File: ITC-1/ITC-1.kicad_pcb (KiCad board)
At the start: 4 copper layers, 46 x 46 mm, 71 parts, among them K1 кнопка, K2 кнопка, X1 крепеж, X2 крепеж, X3 крепеж, X4 крепеж

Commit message: закончена трассировка, сформированы герберы
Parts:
- added C3: Конденсатор_керамический, N_RLC:Конденсатор_SMD_0603_pnp, F.Cu at (87.5, 86.8)
- added C4: Конденсатор_керамический, N_RLC:Конденсатор_SMD_0603_pnp, F.Cu at (85.8, 67.5)
- added C5: Конденсатор_керамический, N_RLC:Конденсатор_SMD_0603_pnp, F.Cu at (90.8, 67.5)
- added C6: Конденсатор_керамический, N_RLC:Конденсатор_SMD_0603_pnp, F.Cu at (88.0, 67.5)
- added R19: Резистор_0,065Вт, N_RLC:Резистор_SMD_0603_0,065_Вт_pnp, F.Cu at (90.2, 72.2)
- added R20: Резистор_0,065Вт, N_RLC:Резистор_SMD_0603_0,065_Вт_pnp, F.Cu at (88.0, 72.2)
- added R24: Резистор_0,065Вт, N_RLC:Резистор_SMD_0603_0,065_Вт_pnp, F.Cu at (85.8, 72.2)
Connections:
- A1 pad 5: /3-LION -> /ADC1-CH3
- A1 pad 6: /2-LION -> /ADC1-CH6
- A1 pad 7: /1-LION -> /ADC1-CH7
- R38 pad 1: /3-LION -> /ADC1-CH3
- R39 pad 1: /2-LION -> /ADC1-CH6
- R40 pad 1: /1-LION -> /ADC1-CH7
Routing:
- net /ADC1-CH3: track 0.00 -> 22.5 mm, vias 0 -> 1
- net /ADC1-CH6: track 0.00 -> 17.8 mm, vias 0 -> 1
- net /1-LION: track 10.9 -> 27.4 mm
- net /GND: track 130.8 -> 147.1 mm
- net /2-LION: track 16.6 -> 30.4 mm
- net /ADC1-CH7: track 0.00 -> 10.4 mm, vias 0 -> 1
- net /3-LION: track 13.9 -> 16.2 mm
- net /3V3: track 47.4 -> 48.8 mm
- net Net-(HL1-Pad2): track 9.19 -> 7.94 mm

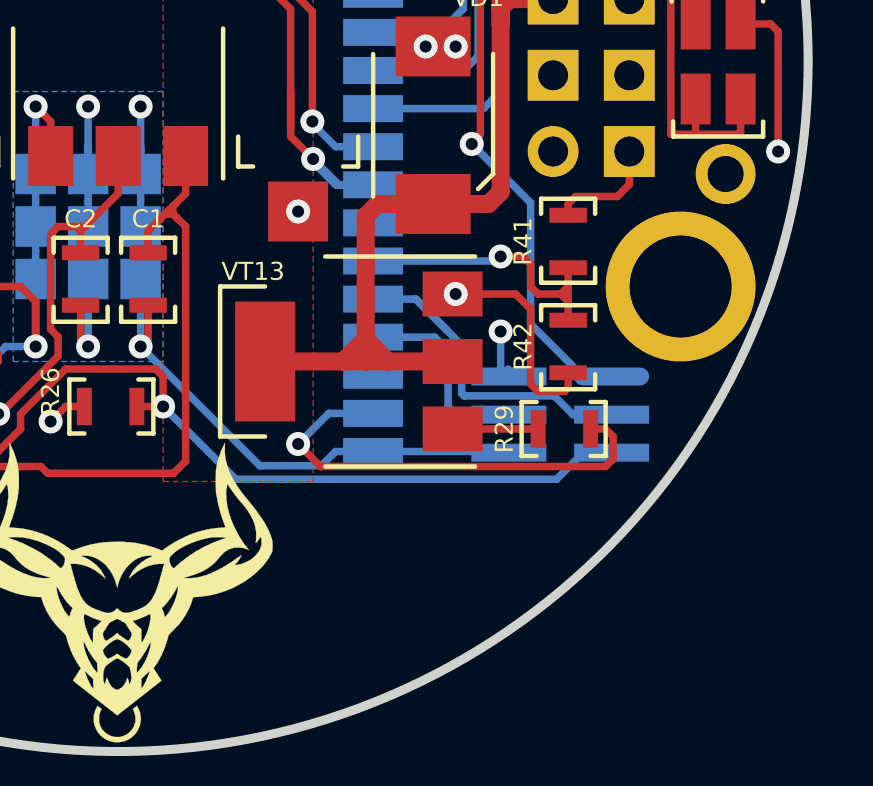
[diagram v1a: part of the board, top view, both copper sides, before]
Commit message: исправлено заземление транзистора, подготовлены файлы производства
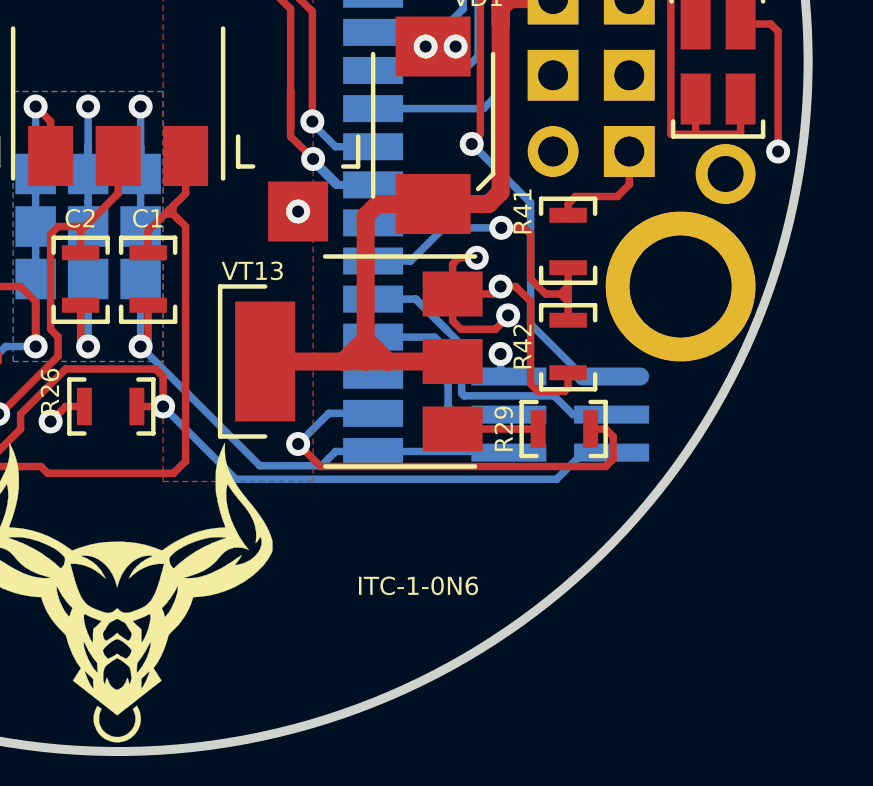
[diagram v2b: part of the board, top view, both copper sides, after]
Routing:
- net /GND: track 147.1 -> 152.5 mm, vias 20 -> 22
- net /CHARGE-SENS: track 9.85 -> 11.1 mm
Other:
- board text added: "ITC-1-0N6"

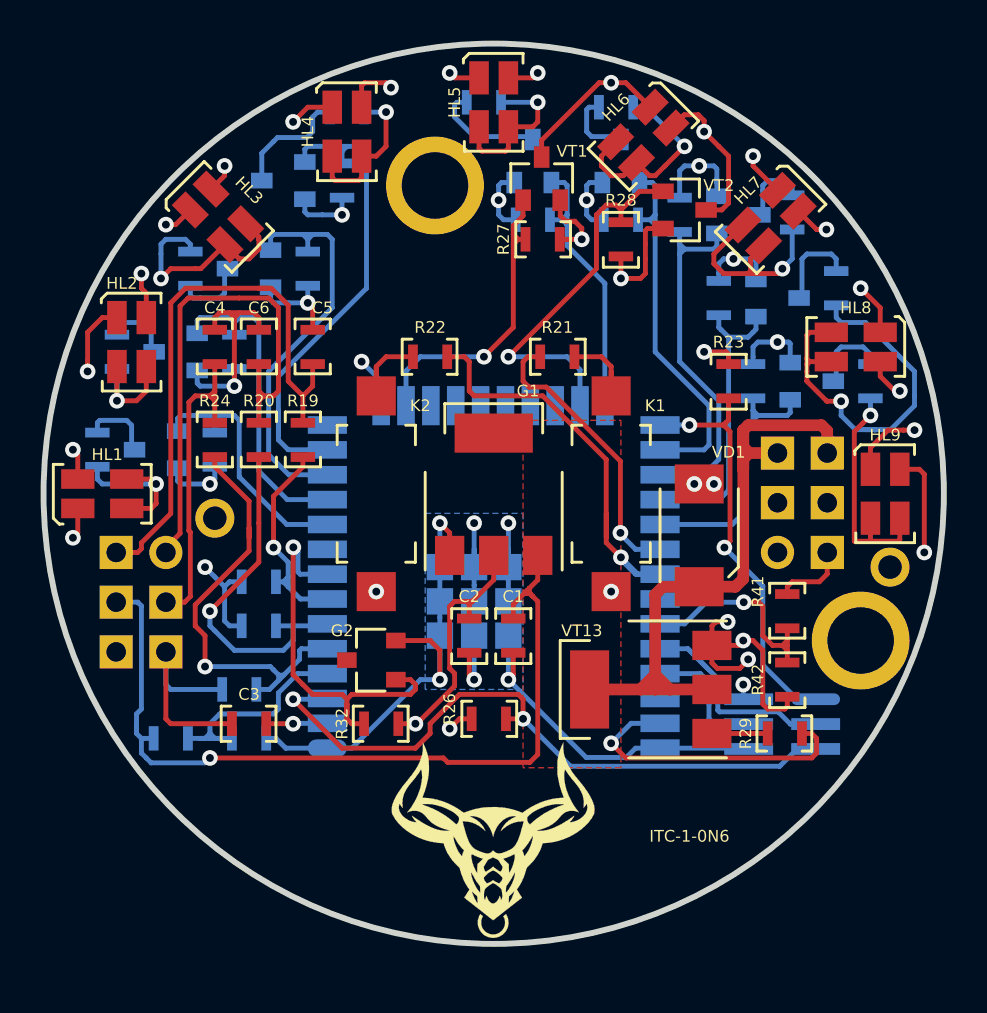
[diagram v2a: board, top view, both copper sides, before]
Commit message: PCB: транзистор N-канал, утолщены дорожки, кнопка BOOT, заменен прог.
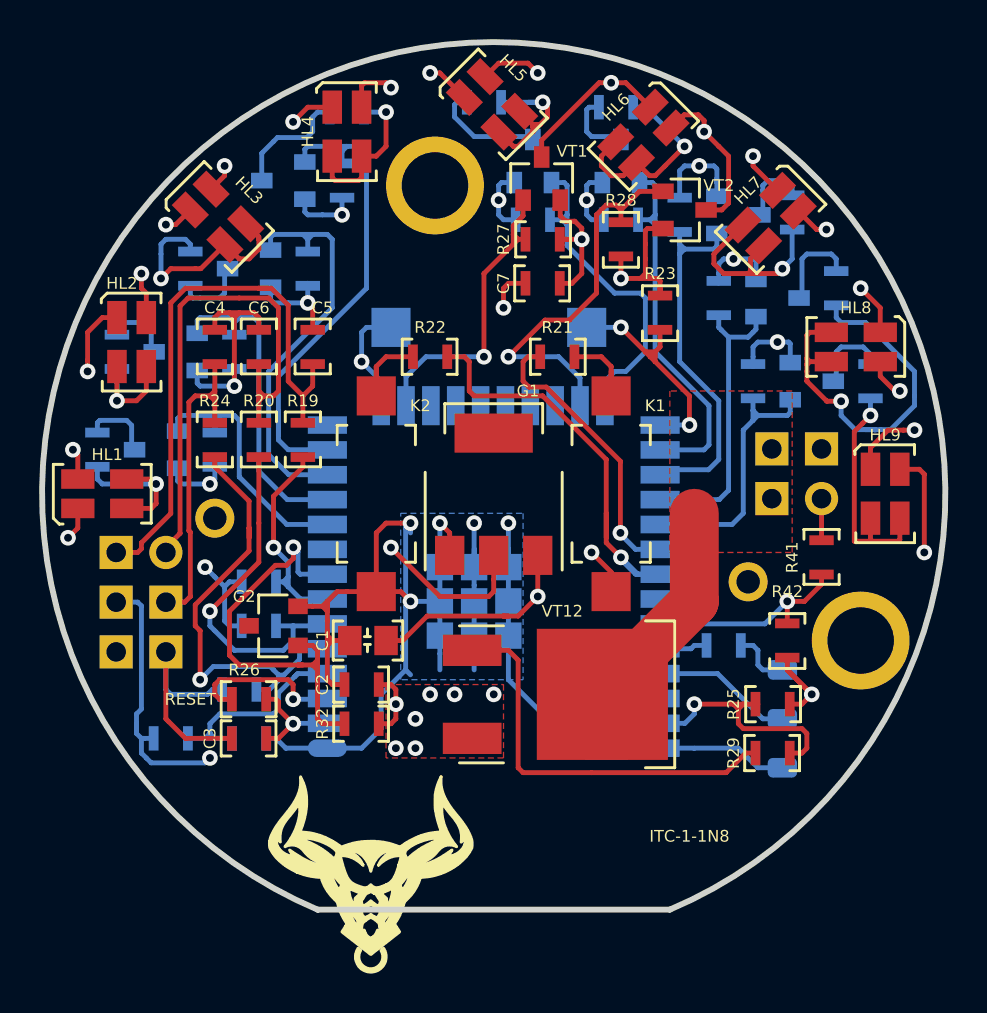
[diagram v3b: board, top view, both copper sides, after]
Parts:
- removed VD1: Диод_шоттки, N_VD_HL:Диод_SMB_pnp
- removed VT13: Транзистор_NPN_1Б-2(4)К-3Э_0, N_VD_HL:Транзистор_NPN_SOT223_pnp
- removed XP1: Вилка_PLD6_ПРОГ_STM, N_X:Вилка_PLLD6_угловая_вертикальная
- removed XP4: Вилка_PLS6, N_X:Вилка_PLD6_вертикальная
- added C7: Конденсатор_керамический, N_RLC:Конденсатор_SMD_0603_pnp, F.Cu at (102.5, 64.2)
- added K3: кнопка, N_X:Кнопка_FSMSM, B.Cu at (104.8, 66.5)
- added R25: Резистор_0,065Вт, N_RLC:Резистор_SMD_0603_0,065_Вт_pnp, F.Cu at (114.2, 85.8)
- added R30: Резистор_0,065Вт, N_RLC:Резистор_SMD_0603_0,065_Вт_pnp, B.Cu at (111.8, 82.8)
- added VT12: Транзистор_полевой_N-канал, N_VD_HL:Транзистор_N-канал_dpak_DS, F.Cu at (101.2, 85.2)
- added X6: Вилка_PLS4, N_X:Вилка_PLD4_вертикальная, B.Cu at (116.8, 75.2)
- added X7: Check_point, N_X:Пробник, B.Cu at (114.8, 84.0)
- added X8: Check_point, N_X:Пробник, B.Cu at (114.8, 86.5)
- added X9: Check_point, N_X:Пробник, B.Cu at (114.8, 89.0)
- C1: footprint N_RLC:Конденсатор_SMD_0603_pnp -> N_RLC:Конденсатор_SMD_IEC_0805
- moved D1 33.5 mm to (127.8, 65.0)
- moved R26 12.3 mm to (87.5, 85.5), turned to 180 degrees
- moved X3 7.29 mm to (113.0, 79.5)
- moved C1 6.50 mm to (94.5, 82.5), turned to 180 degrees
- moved D2 6.49 mm to (93.8, 94.5)
- moved C2 6.04 mm to (93.2, 84.8), turned to 180 degrees
- moved G2 5.30 mm to (88.8, 81.8)
- moved R23 4.95 mm to (108.5, 65.8)
- moved R41 3.26 mm to (116.8, 78.2)
- moved R42 2.00 mm to (115.0, 82.5)
- moved HL5 1.25 mm to (98.5, 54.8), turned to 45 degrees
- moved R29 1.18 mm to (114.2, 88.2)
- moved R32 1.00 mm to (93.2, 86.8)
- moved C3 0.75 mm to (87.5, 87.5)
- renumbered XP5 to X5
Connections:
- A1 pad 14: Net-(A1-Pad14) -> (no net)
- A1 pad 17: Net-(A1-Pad17) -> (no net)
- A1 pad 18: Net-(A1-Pad18) -> (no net)
- A1 pad 19: Net-(A1-Pad19) -> (no net)
- A1 pad 20: Net-(A1-Pad20) -> (no net)
- A1 pad 21: Net-(A1-Pad21) -> (no net)
- A1 pad 22: Net-(A1-Pad22) -> (no net)
- A1 pad 32: Net-(A1-Pad32) -> (no net)
- A1 pad 36: Net-(A1-Pad36) -> (no net)
- A1 pad 9: Net-(A1-Pad9) -> (no net)
- G2 pad 3: Net-(G2-Pad3) -> (no net)
- X1 pad 1: Net-(X1-Pad1) -> (no net)
- X2 pad 1: Net-(X2-Pad1) -> (no net)
- X3 pad 1: Net-(X3-Pad1) -> (no net)
- X4 pad 1: Net-(X4-Pad1) -> (no net)
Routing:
- net /4-LION: track 98.7 -> 63.0 mm, vias 3 -> 2
- net /EN_RESET: track 34.3 -> 8.08 mm, vias 2 -> 1
- net /MOTOR-GND: track 35.4 -> 11.2 mm
- net /GND: track 152.5 -> 174.0 mm, vias 22 -> 25
- net Net-(R29-Pad2): track 2.75 -> 20.8 mm
- net /3V3: track 49.2 -> 32.3 mm, vias 7 -> 5
- net /BOOT_SEL: track 21.0 -> 12.3 mm
- net /BOOT_UART_RX: track 11.0 -> 2.32 mm
- net /MOTOR-DRIVE: track 15.4 -> 12.6 mm
- net /LED_5: track 14.1 -> 16.9 mm
- net Net-(R30-Pad2): track 0.00 -> 2.58 mm
- net Net-(HL5-Pad2): track 10.5 -> 8.58 mm
- net /BUTT_1: track 14.7 -> 16.4 mm
- net Net-(R41-Pad2): track 3.91 -> 2.25 mm
- net /ADC1-CH4: track 20.2 -> 21.6 mm
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- added copper zone on F.Cu, net /GND
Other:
- board size 46 x 46 mm -> 46.2 x 44.3 mm
- net class PWR: trace_width 0.6 -> 2.5
- board text added: "BOOT"
- board text added: "GND"
- board text added: "ITC-1-1N8"
- board text added: "RESET"
- board text added: "RX"
- board text added: "TX"
- board text removed: "ITC-1-0N6"

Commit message: ITC-1-1 исправлен проект
добавлены стабилизаторы на DIN и LI4, усилены дорожки, фаски с двух сторон
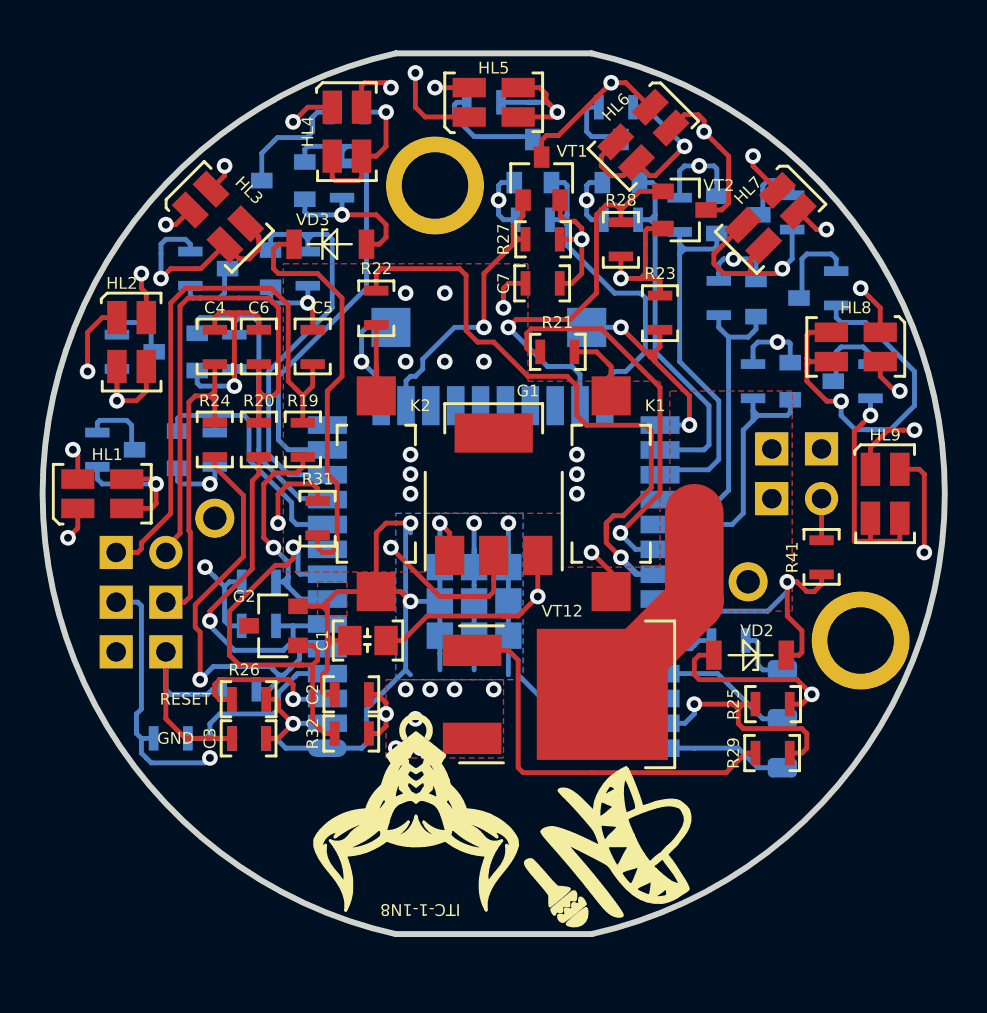
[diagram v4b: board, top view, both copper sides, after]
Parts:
- removed R42: Резистор_0,065Вт, N_RLC:Резистор_SMD_0603_0,065_Вт_pnp
- added R31: Резистор_0,065Вт, N_RLC:Резистор_SMD_0603_0,065_Вт_pnp, F.Cu at (91.0, 76.2)
- added VD2: Стабилитрон_1N5352BRLG_вертикальный, N_VD_HL:SOD-80, F.Cu at (111.2, 83.2)
- added VD3: Стабилитрон_1N5352BRLG_вертикальный, N_VD_HL:SOD-80, F.Cu at (93.5, 62.2)
- D1: moved to F.Cu
- moved D1 36.4 mm to (105.5, 93.8), turned to 247.5 degrees
- moved D2 3.95 mm to (96.0, 91.2), turned to 180 degrees
- moved R22 3.72 mm to (94.0, 65.5), turned to 270 degrees
- moved HL5 1.03 mm to (98.8, 55.8), turned to 90 degrees
- moved C2 0.71 mm to (92.8, 85.2)
- moved R32 0.71 mm to (92.8, 87.2)
- moved R30 0.35 mm to (112.0, 82.5)
- moved R21 0.25 mm to (103.2, 67.8)
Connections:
- G1 pad 4: (no net) -> /3V3
- X3 pad 1: (no net) -> /MOTOR-GND
- X4 pad 1: (no net) -> /GND
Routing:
- net Net-(R31-Pad2): track 0.00 -> 21.3 mm
- net /4-LION: track 63.0 -> 82.0 mm, vias 2 -> 3
- net /BUTT_2: track 22.8 -> 34.8 mm
- net /GND: track 174.0 -> 181.9 mm, vias 25 -> 26
- net /BUTT_1: track 16.4 -> 20.5 mm
- net /CHARGE-SENS: track 11.5 -> 15.1 mm
- net /3V3-GREEN: track 102.4 -> 100.4 mm
- net /3V3-RED: track 103.1 -> 104.9 mm
- net /ADC1-CH7: track 10.4 -> 11.5 mm
- net /ADC1-CH3: track 23.6 -> 22.8 mm
- net /LED_RED: track 15.7 -> 15.0 mm
- net /ADC1-CH4: track 21.6 -> 21.0 mm
- net /3V3: track 32.3 -> 32.0 mm, vias 5 -> 16
- added copper zone on F.Cu, net /3V3
- added copper zone on In2.Cu-VCC, net /4-LION
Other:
- board size 46.2 x 44.3 mm -> 46.1 x 45 mm
- board text added: "DIN"
- board text added: "LI1"
- board text added: "LI2"
- board text added: "LI3"
- board text added: "LI4"
- board text added: "MGND"

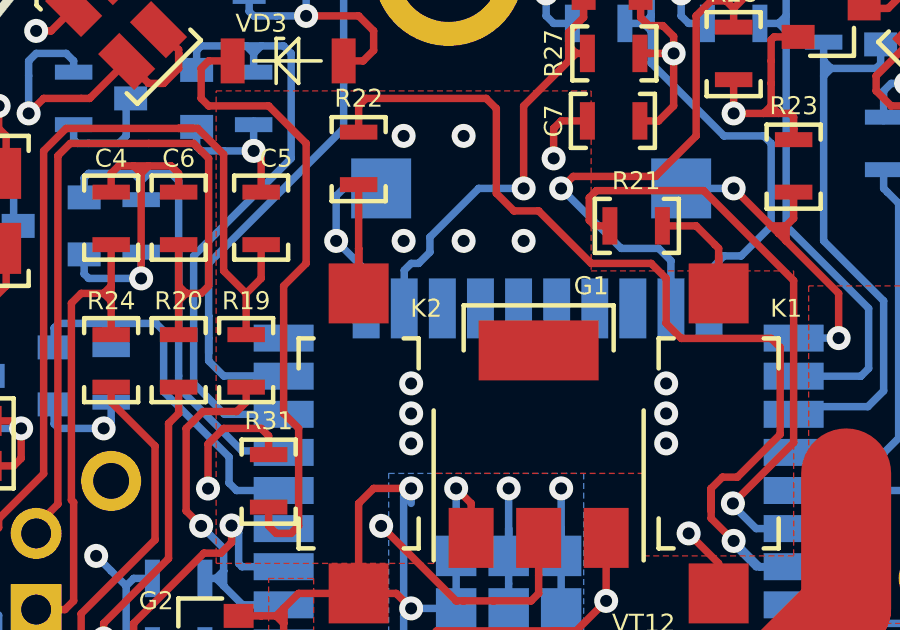
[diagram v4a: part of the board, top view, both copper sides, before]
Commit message: на esp32 убраны запрещенные площадки, сформированы gerber-файлы
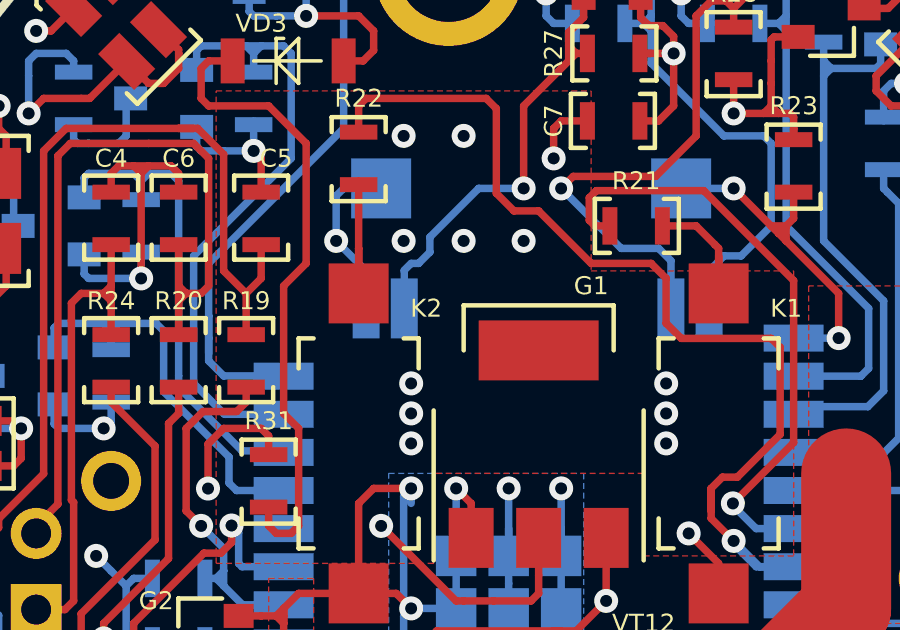
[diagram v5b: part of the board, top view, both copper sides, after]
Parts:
- A1: footprint N_A:ESP32_WROOM32_pnp -> N_A:ESP32_WROOM32_pnp_noSD
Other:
- board text added: "G"
- board text added: "R"
